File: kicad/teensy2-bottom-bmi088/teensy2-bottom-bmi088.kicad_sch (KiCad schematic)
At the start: 7 parts, among them J1 Conn_01x14_Socket, J2 Conn_01x14_Socket, J3 Conn_01x03_Socket, J4 Conn_01x03_Socket, J5 Conn_01x01_Socket, J6 Conn_01x02_Socket

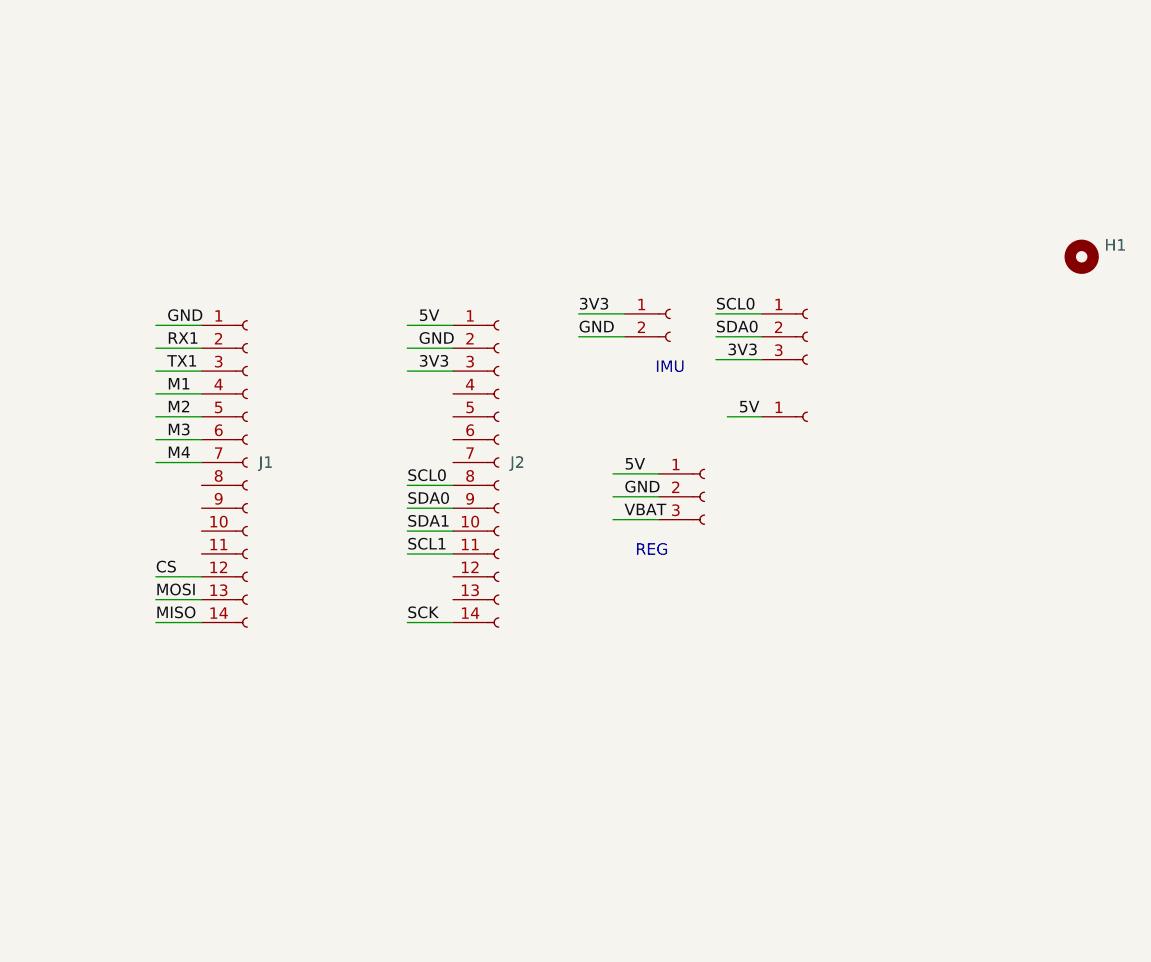
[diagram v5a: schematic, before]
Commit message: modified:   kicad/teensy2-bottom-bmi088/teensy2-bottom-bmi088.kicad_pcb
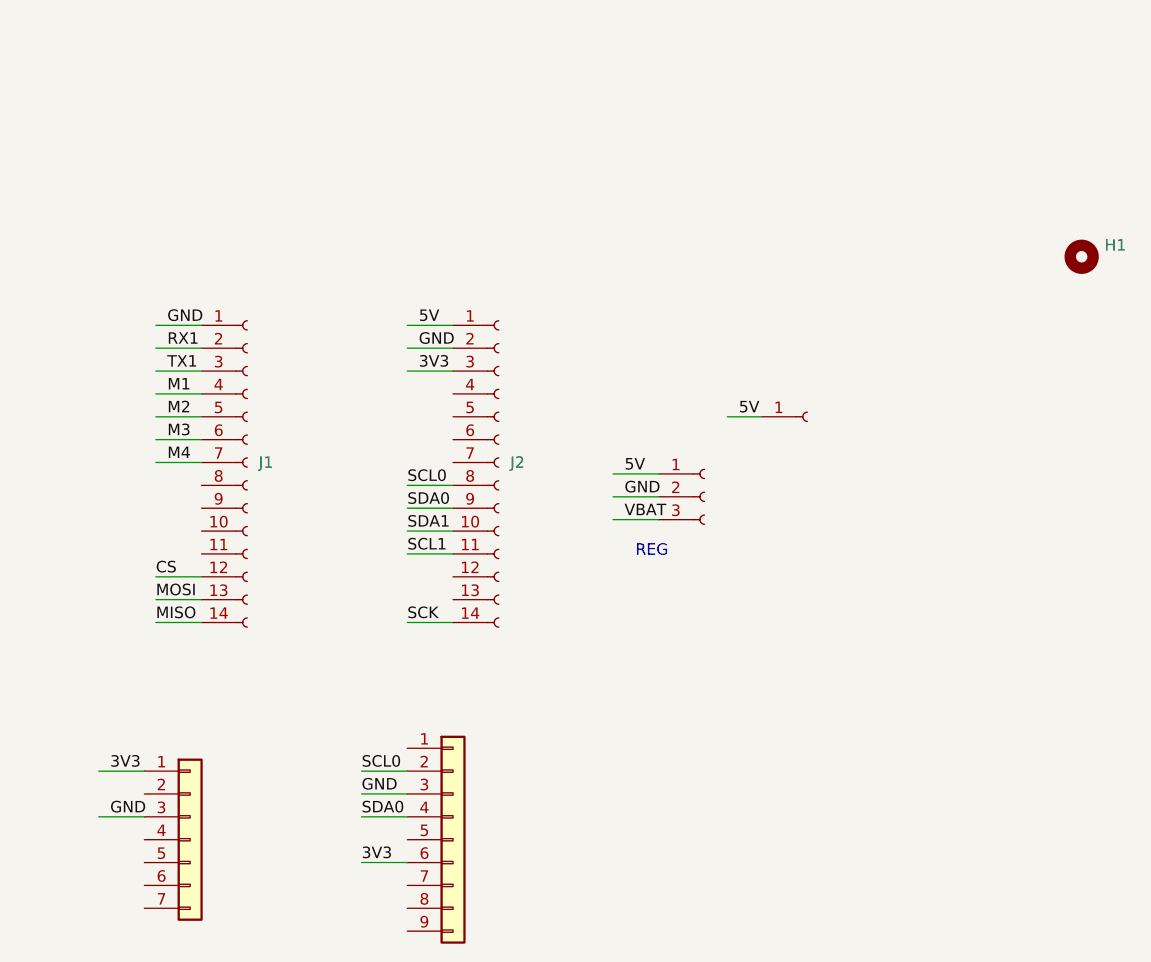
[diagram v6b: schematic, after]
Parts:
- removed J3: Conn_01x03_Socket, Connector_PinSocket_2.54mm:PinSocket_1x03_P2.54mm_Vertical, symbol Connector:Conn_01x03_Socket
- removed J6: Conn_01x02_Socket, Connector_PinSocket_2.54mm:PinSocket_1x02_P2.54mm_Vertical, symbol Connector:Conn_01x02_Socket
- added J7: Conn_01x07, Connector_PinHeader_1.27mm:PinHeader_1x07_P1.27mm_Vertical, symbol Connector_Generic:Conn_01x07
- added J8: Conn_01x09, Connector_PinHeader_1.27mm:PinHeader_1x09_P1.27mm_Vertical, symbol Connector_Generic:Conn_01x09
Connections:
- net 3V3: now also J7.1 (Pin_1), J8.6 (Pin_6)
- net GND: now also J7.3 (Pin_3), J8.3 (Pin_3)
- net SCL0: now also J8.2 (Pin_2)
- net SDA0: now also J8.4 (Pin_4)
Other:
- note removed: "IMU"

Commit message: modified:   kicad/teensy2-bottom-bmi088/teensy2-bottom-bmi088.kicad_pcb
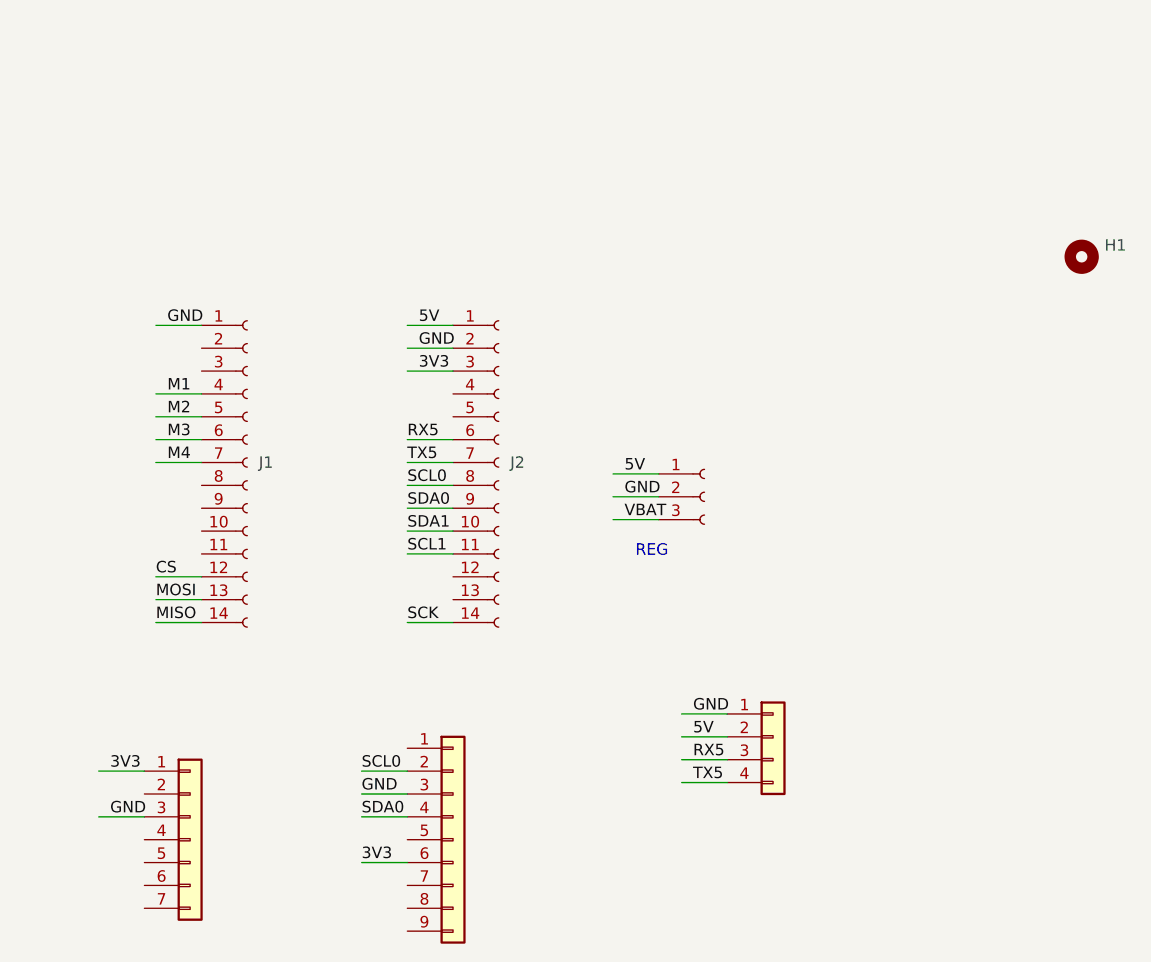
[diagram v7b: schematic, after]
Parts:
- removed J5: Conn_01x01_Socket, Connector_Wire:SolderWirePad_1x01_SMD_1x2mm, symbol Connector:Conn_01x01_Socket
- added J3: Conn_01x04, Connector_PinHeader_2.00mm:PinHeader_1x04_P2.00mm_Vertical, symbol Connector_Generic:Conn_01x04
- J1: value Conn_01x14_Socket -> Conn_01x14
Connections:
- net 5V: now also J3.2 (Pin_2)
- net GND: now also J3.1 (Pin_1)
- net RX5: now reaches J2.6 (Pin_6)
- net RX5: now also J3.3 (Pin_3)
- net TX5: now reaches J2.7 (Pin_7)
- net TX5: now also J3.4 (Pin_4)
- net RX1: no longer names the net of J1.2 (Pin_2)
- net TX1: no longer names the net of J1.3 (Pin_3)
